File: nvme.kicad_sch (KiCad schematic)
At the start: 19 parts, among them J3 Bus_M.2_Socket_M, U1 AP3441SHE-7B, U2 ASEK-32.768KHZ-L-R-T

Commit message: moved power TPs to cm5 sheet
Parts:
- 3V3_M2: symbol Connector:TestPoint -> library:TestPoint
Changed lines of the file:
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@@
 	)
 	(symbol
-		(lib_id "power:PWR_FLAG")
+		(lib_id "library:PWR_FLAG")
 		(at 132.08 119.38 0)
 		(unit 1)
@@
 	)
 	(symbol
-		(lib_id "Connector:TestPoint")
+		(lib_id "library:TestPoint")
 		(at 173.99 120.65 0)
 		(unit 1)

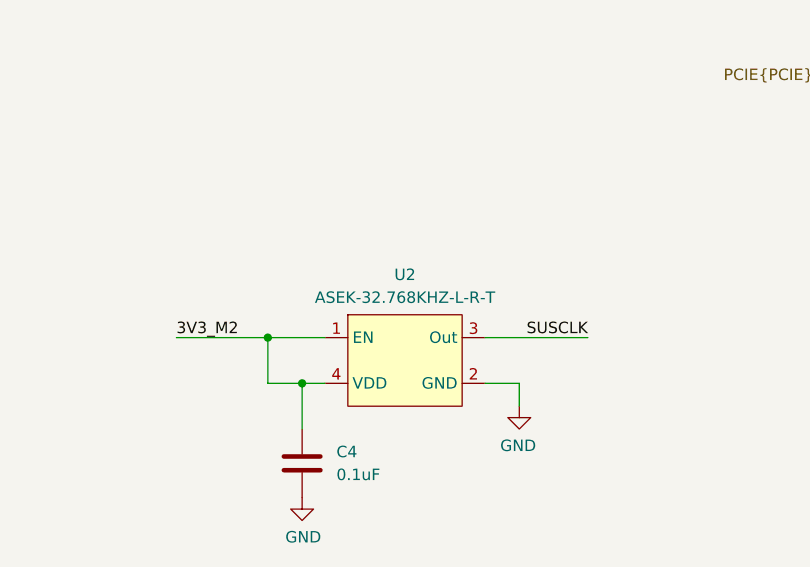
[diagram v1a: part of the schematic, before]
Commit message: silkscreen edits
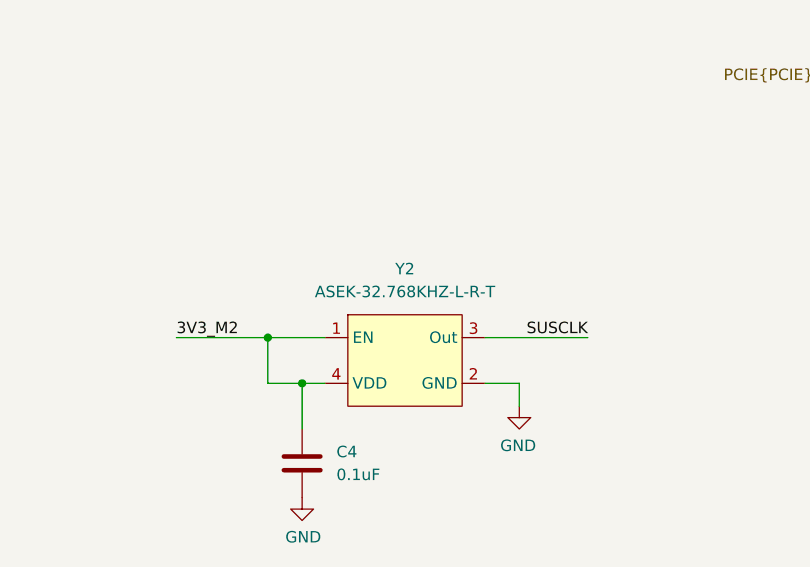
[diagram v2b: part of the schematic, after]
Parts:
- renumbered U2 to Y2
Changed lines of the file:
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@@
 		(dnp no)
 		(fields_autoplaced yes)
-		(property "Reference" "U2"
-			(at 97.79 60.325 0)
+		(property "Reference" "Y2"
+			(at 97.79 59.69 0)
 			(effects
 				(font
@@
 		)
 		(property "Value" "ASEK-32.768KHZ-L-R-T"
-			(at 97.79 62.865 0)
+			(at 97.79 62.23 0)
 			(effects
 				(font
@@
 			(project "CUTIE-CITRUS"
 				(path "/40af415e-5e3a-41a5-ab07-08c2181863e4/7953df6c-8185-4fff-8cd2-b6d3791adbaa"
-					(reference "U2")
+					(reference "Y2")
 					(unit 1)
 				)

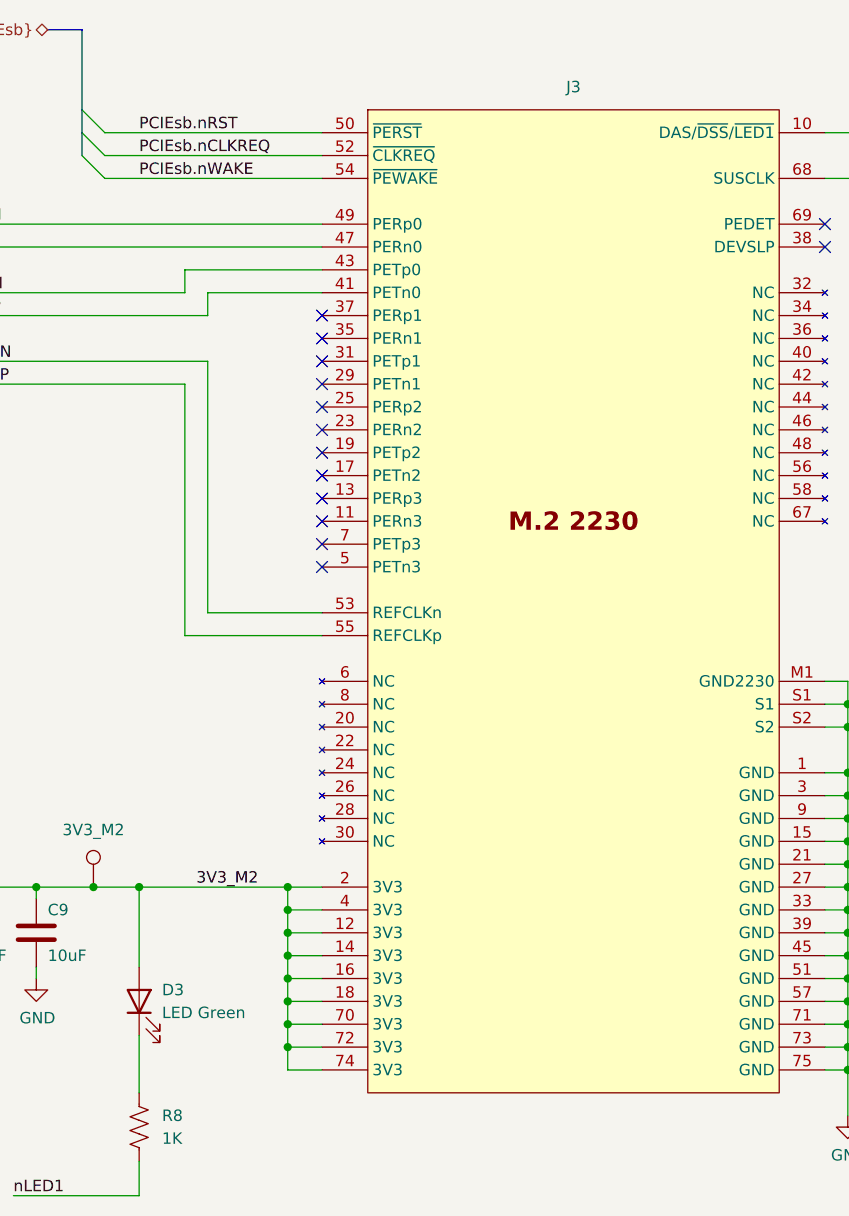
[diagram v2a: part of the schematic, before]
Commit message: redid gpio layout, removed one temp sensor, bom
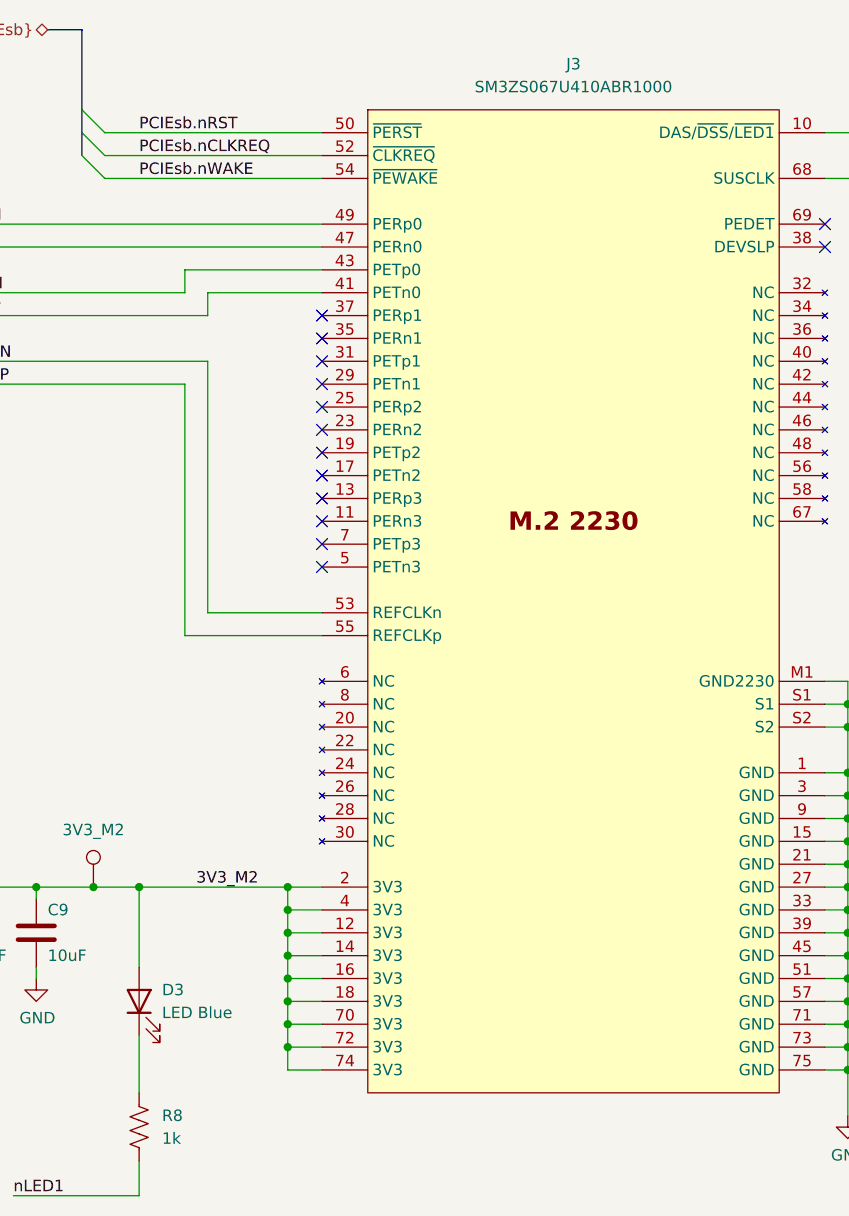
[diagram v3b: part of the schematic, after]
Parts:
- 3V3_M2: now left out of the parts list
- C1, C2, C6, C7, C8, C9: Field4 Digikey -> (none); Field5 490-14381-1-ND -> (none); Field6 GRM21BR71A106KA73L -> (none); Field7 Murata -> (none); Field8 111893011 -> (none); Manufacturer (none) -> Murata Electronics; Manufacturer Product Number (none) -> GRM21BR71A106KA73L; Part Description 10uF 10% 10V Ceramic Capacitor X7R 0805 (2012 Metric) -> (none)
- C3, C4: Field4 Farnell -> (none); Field5 2611911 -> (none); Field6 RM EMK105 B7104KV-F -> (none); Field7 TAIYO YUDEN EUROPE GMBH -> (none); Field8 110091611 -> (none); Manufacturer (none) -> KEMET; Manufacturer Product Number (none) -> C0402C104K4RACTU; Part Description 0.1uF 10% 16V Ceramic Capacitor X7R 0402 (1005 Metric) -> (none)
- C5: Manufacturer (none) -> KEMET; Manufacturer Product Number (none) -> C0402C472J5RECTU; Part Description 4.7nF capacitor 0402 -> (none)
- D3: value LED Green -> LED Blue; Field4 Digikey -> (none); Field5 LTST-S270KGKT -> (none); Field6 SML-A12M8TT86N -> (none); Field7 Rohm -> (none); Field8 650263301 -> (none); Manufacturer (none) -> Lite-On Inc.; Manufacturer Product Number (none) -> LTST-S270TBKT; Part Description Green 572nm LED Indication - Discrete 2.2V 2-SMD, No Lead -> (none)
- J3: value Bus_M.2_Socket_M -> SM3ZS067U410ABR1000; Field5 MTSSD03-67MSW337 -> (none); Field6 MTSSD03-67MSW337 -> (none); Field7 MTCONN -> (none); Manufacturer (none) -> JAE Electronics; Manufacturer Product Number (none) -> SM3ZS067U410ABR1000; Part Description M.2 M Key connector -> (none)
- L1: footprint Capacitor_SMD:C_0402_1005Metric -> Inductor_SMD:L_Vishay_IHLP-1616; Field5 SRP5030CC-2R2M -> (none); Field6 SRP5030CC-2R2M -> (none); Field7 Bourns -> (none); Manufacturer (none) -> Vishay Dale; Manufacturer Product Number (none) -> IHLP1616BZER1R0M01; Part Description Inductor, SMT, 2520, 2u2, IRMS=7A, ISAT=8A, DCR=0.032R -> (none)
- R5: Field4 Farnell -> (none); Field6 MCR01MZPF1003 -> (none); Field7 Rohm -> (none); Manufacturer (none) -> YAGEO; Manufacturer Product Number (none) -> RC0402FR-07100KL; Part Description Resistor 100K M1005 1% 63mW -> (none)
- R6: Field4 Farnell -> (none); Field6 MCR01MZPF1002 -> (none); Field7 Rohm -> (none); Manufacturer (none) -> Vishay Dale; Manufacturer Product Number (none) -> CRCW040210K0FKED; Part Description Resistor 10K M1005 1% 63mW -> (none)
- R7: Field4 Farnell -> (none); Manufacturer (none) -> Vishay Dale; Manufacturer Product Number (none) -> CRCW04022K20FKED; Part Description Resistor 2.2K M1005 1% 63mW -> (none)
- R8: value 1K -> 1k; Field4 Farnell -> (none); Field5 9239235 -> (none); Field6 RK73H1ETTP1001F -> (none); Field7 KOA EUROPE GMBH -> (none); Field8 125049511 -> (none); Manufacturer (none) -> YAGEO; Manufacturer Product Number (none) -> RC0402JR-071KL; Part Description Resistor 1K M1005 1% 63mW -> (none)
- U1: Field5 AP3441SHE-7B -> (none); Field6 AP3441SHE-7B -> (none); Field7 Diodes -> (none); Manufacturer (none) -> Diodes Incorporated; Manufacturer Product Number (none) -> AP3441SHE-7B; Part Description 3A DC-DC converter -> (none)
- Y2: Field5 ASEK-32.768KHZ-L-R-T -> (none); Field6 ASEK-32.768KHZ-L-R-T -> (none); Field7 abracon -> (none); Manufacturer (none) -> Abracon LLC; Manufacturer Product Number (none) -> ASEK-32.768KHZ-L-R-T; Part Description 32KHz Xtal oscilator -> (none)

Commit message: fixes for fab
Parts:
- L1: Manufacturer Product Number IHLP1616BZER1R0M01 -> IHLP1616BZER2R2M11
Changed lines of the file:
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@@
 			)
 		)
-		(property "Manufacturer Product Number" "IHLP1616BZER1R0M01"
+		(property "Manufacturer Product Number" "IHLP1616BZER2R2M11"
 			(at 106.68 120.65 90)
 			(effects
